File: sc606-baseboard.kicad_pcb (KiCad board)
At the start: 6 copper layers, 100 x 90 mm, 420 parts, among them IC1 TPS54561DPRT, IC2 TPS7A0518PDBVT, J1 PJ-202A, J10 WE_632723300011, J11 WE_632723300011, J12 U_FL-R-SMT-1_10_, J13 WE_632723300011, J14 CONMMCX002-SMD-T, J2 WE_68715014522, J3 F52R-1A7H1-11020, J4 46756-1001, J5 U_FL-R-SMT-1_10_, J6 U_FL-R-SMT-1_10_, J7 DM3AT-SF-PEJM5, J8 693022010811, J9 0473460001, M1 SC606T, Q1 BSS138APW, Q2 BSS138-7-F, Q3 BSS138APW, Q4 BSS138APW, Q5 BSS138APW, Q6 BSS138APW, Q7 BSS138-7-F, Q8 BSS138-7-F, SW1 1X03, U1 AP62301WU-7, U10 NCP163ASN330T1G, U11 EMIF06-MSD02N16, U12 FSUSB30MUX, U13 FT232RQ-REEL, U15 USB57442G, U2 AP62301WU-7, U3 AP62301WU-7, U4 74LVC1G123GN, U5 NTS0102GT, U6 PCA9547BS, U7 LT9611UXC, U8 NTS0102GT, U9 TPD13S523PWR, Y1 ABM8G-24.000MHZ-18-D2Y-T, Y2 ABM8G-25.000MHZ-B4Y-T

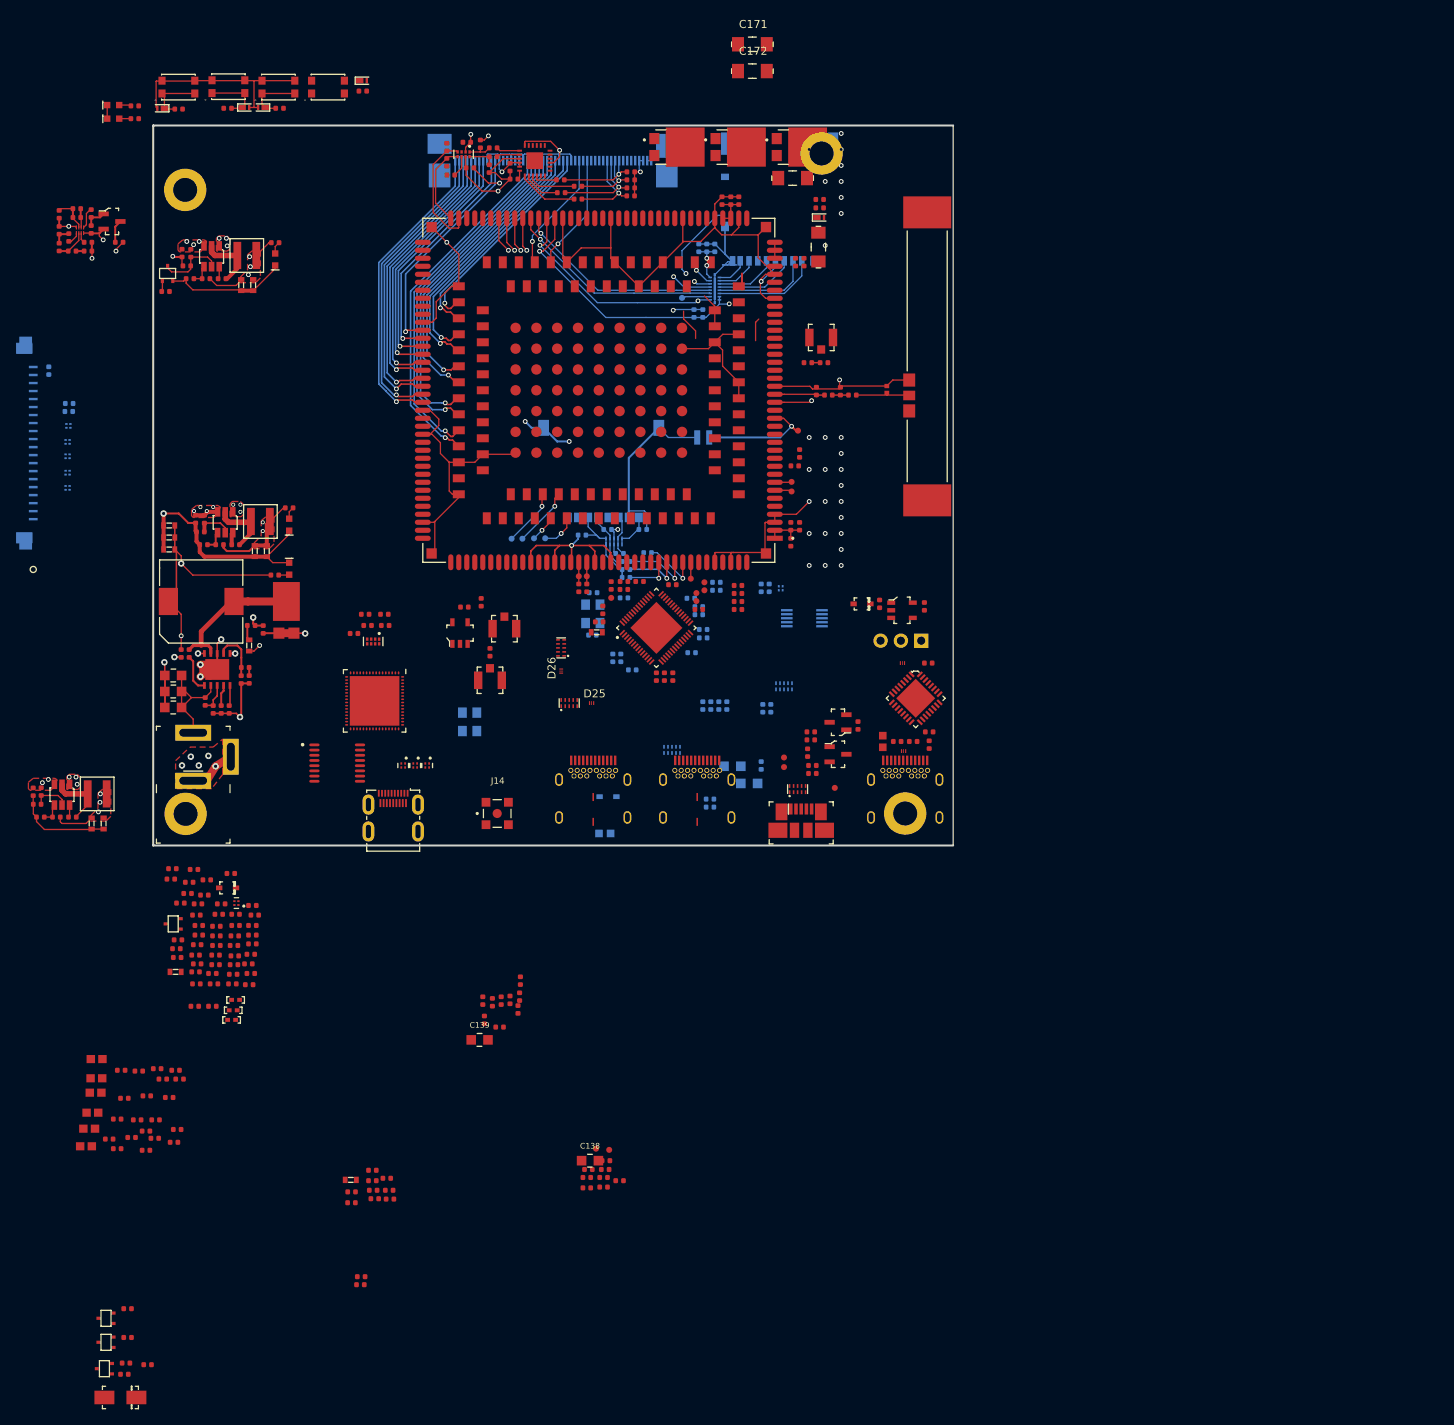
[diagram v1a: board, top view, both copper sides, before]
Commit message: All components placed on board
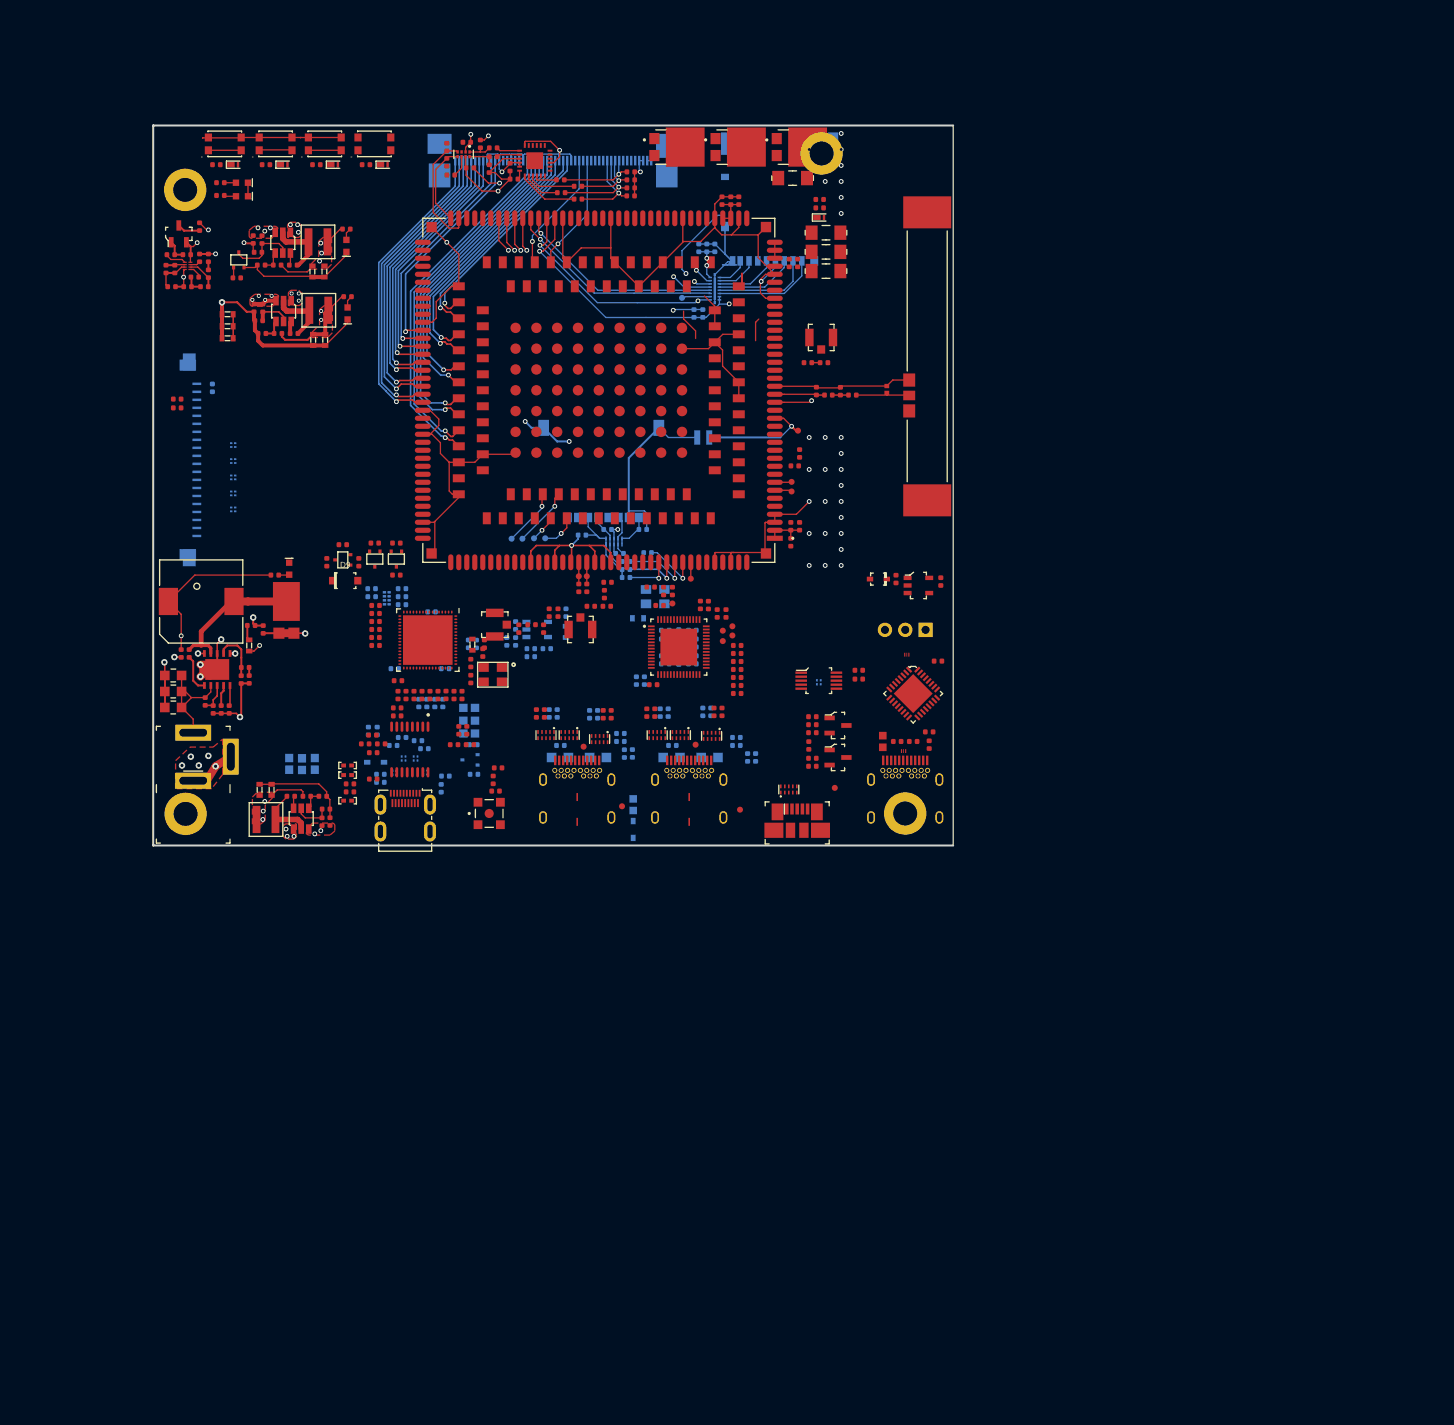
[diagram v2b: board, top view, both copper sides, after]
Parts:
- added C142: C_1u_0402, sc606-baseboard-footprints:0402-cap, F.Cu at (118.1, 120.3)
- added C143: C_1u_0402, sc606-baseboard-footprints:0402-cap, F.Cu at (117.8, 123.2)
- added R138: R_0R_0402, sc606-baseboard-footprints:0402-res, F.Cu at (124.5, 100.9)
- added R139: R_0R_0402, sc606-baseboard-footprints:0402-res, F.Cu at (125.6, 100.9)
- added R140: R_0R_0402, sc606-baseboard-footprints:0402-res, F.Cu at (117.5, 121.8)
- C102, C103, C120, C125, C131, C138, C139, C47, C48, C49, C50, C51, C52, C54, C55, C56, C59, C60, C61, C62, C63, C64, C65, C66, C67, C68, C70, C73, C74, C75, C76, C77, C78, C79, C80, C85, C86, C87, C88, C94, C95, C96, C99, D10, L13, L14, L15, L16, L17, L18, L19, L21, L5, L6, L7, Q3, R113, R122, R123, R124, R125, R131, R132, R134, R135, R71, R72, R73, R74, R81, R82, R84, R85, R89, R90, R92, R94, U10, U8: moved to B.Cu
- C108, C132, C133, C135, C148, C150, D31, D32, R107, R119, R55, R56, U12, Y1: moved to F.Cu
- D25, D26: value PESD5V0C2BDFZ -> PUSB3F96X_PASS; footprint sc606-baseboard-footprints:DFN0603-3 -> sc606-baseboard-footprints:PUSB3F96X
- D9: value S1G -> 1N4148W-7-F; footprint sc606-baseboard-footprints:DO-214AC -> antmicro-footprints:SOD-123
- moved D9 105.9 mm to (99.0, 96.9), turned to 0 degrees
- moved R80 105.8 mm to (98.7, 92.4)
- moved R79 105.6 mm to (100.7, 94.6), turned to 90 degrees
- moved Q4 105.4 mm to (98.7, 94.3)
- moved R78 104.8 mm to (105.4, 92.2)
- moved Q6 104.4 mm to (105.4, 94.2), turned to 270 degrees
- moved R83 102.8 mm to (96.7, 94.6), turned to 90 degrees
- moved Q5 100.7 mm to (102.7, 94.2), turned to 270 degrees
- moved R77 100.6 mm to (102.7, 92.2)
- moved C91 84.4 mm to (120.7, 102.9), turned to 270 degrees
- moved C89 84.1 mm to (123.8, 102.9), turned to 270 degrees
- moved R93 82.4 mm to (131.4, 98.6), turned to 270 degrees
- moved C93 81.8 mm to (131.8, 97.1)
- moved C98 78.6 mm to (131.7, 100.1)
- moved C101 76.8 mm to (129.7, 100.1)
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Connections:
- net /display module/SoMtoLT__SCL renamed /display module/SoMtoLT_SCL
- C103 pad 2: Net-(C103-Pad2) -> /USB_HUB_Connectors/5V0_USB
- C138 pad 2: Net-(C103-Pad2) -> /USB_HUB_Connectors/5V0_USB
- C139 pad 2: Net-(C103-Pad2) -> /USB_HUB_Connectors/5V0_USB
- C151 pad 2: Net-(C151-Pad2) -> /USB_HUB_Connectors/5V0_USB
- C169 pad 2: Net-(C151-Pad2) -> /USB_HUB_Connectors/5V0_USB
- C170 pad 2: Net-(C151-Pad2) -> /USB_HUB_Connectors/5V0_USB
- C171 pad 1: (no net) -> V_SOM
- C172 pad 1: (no net) -> V_SOM
- C89 pad 1: ANT-WIFI -> Net-(C89-Pad1)
- D25 pad 1: /USB_HUB_Connectors/USB_C1_D_P -> /USB_HUB_Connectors/USB_C1_D1_N
- D25 pad 2: /USB_HUB_Connectors/USB_C1_D_N -> /USB_HUB_Connectors/USB_C1_D1_P
- D26 pad 1: /USB_HUB_Connectors/USB_C2_D_P -> /USB_HUB_Connectors/USB_C2_SS_C_TX1_N
- D26 pad 2: /USB_HUB_Connectors/USB_C2_D_N -> /USB_HUB_Connectors/USB_C2_SS_C_TX1_P
- D27 pad 1: /USB_HUB_Connectors/USB_C1_SS_RX2_P -> /USB_HUB_Connectors/USB_C1_SS_C_TX2_N
- D27 pad 10: /USB_HUB_Connectors/USB_C1_SS_RX2_P -> /USB_HUB_Connectors/USB_C1_SS_C_TX2_N
- D27 pad 2: /USB_HUB_Connectors/USB_C1_SS_RX2_N -> /USB_HUB_Connectors/USB_C1_SS_C_TX2_P
- D27 pad 4: /USB_HUB_Connectors/USB_C1_SS_TX2_P -> /USB_HUB_Connectors/USB_C1_SS_C_RX2_P
- D27 pad 5: /USB_HUB_Connectors/USB_C1_SS_TX2_N -> /USB_HUB_Connectors/USB_C1_SS_C_RX2_N
- D27 pad 6: /USB_HUB_Connectors/USB_C1_SS_TX2_N -> /USB_HUB_Connectors/USB_C1_SS_C_RX2_N
- D27 pad 7: /USB_HUB_Connectors/USB_C1_SS_TX2_P -> /USB_HUB_Connectors/USB_C1_SS_C_RX2_P
- D27 pad 9: /USB_HUB_Connectors/USB_C1_SS_RX2_N -> /USB_HUB_Connectors/USB_C1_SS_C_TX2_P
- D28 pad 1: /USB_HUB_Connectors/USB_C1_SS_TX1_P -> /USB_HUB_Connectors/USB_C1_SS_C_TX1_N
- D28 pad 10: /USB_HUB_Connectors/USB_C1_SS_TX1_P -> /USB_HUB_Connectors/USB_C1_SS_C_TX1_N
- D28 pad 2: /USB_HUB_Connectors/USB_C1_SS_TX1_N -> /USB_HUB_Connectors/USB_C1_SS_C_TX1_P
- D28 pad 4: /USB_HUB_Connectors/USB_C1_SS_RX1_P -> /USB_HUB_Connectors/USB_C1_SS_C_RX1_N
- D28 pad 5: /USB_HUB_Connectors/USB_C1_SS_RX1_N -> /USB_HUB_Connectors/USB_C1_SS_C_RX1_P
- D28 pad 6: /USB_HUB_Connectors/USB_C1_SS_RX1_N -> /USB_HUB_Connectors/USB_C1_SS_C_RX1_P
- D28 pad 7: /USB_HUB_Connectors/USB_C1_SS_RX1_P -> /USB_HUB_Connectors/USB_C1_SS_C_RX1_N
- D28 pad 9: /USB_HUB_Connectors/USB_C1_SS_TX1_N -> /USB_HUB_Connectors/USB_C1_SS_C_TX1_P
- D31 pad 1: /USB_HUB_Connectors/USB_C2_SS_TX2_P -> /USB_HUB_Connectors/USB_C2_D1_N
- D31 pad 10: /USB_HUB_Connectors/USB_C2_SS_TX2_P -> /USB_HUB_Connectors/USB_C2_D1_N
- D31 pad 2: /USB_HUB_Connectors/USB_C2_SS_TX2_N -> /USB_HUB_Connectors/USB_C2_D1_P
- D31 pad 4: /USB_HUB_Connectors/USB_C2_SS_RX2_P -> /USB_HUB_Connectors/USB_C2_D2_N
- D31 pad 5: /USB_HUB_Connectors/USB_C2_SS_RX2_N -> /USB_HUB_Connectors/USB_C2_D2_P
- D31 pad 6: /USB_HUB_Connectors/USB_C2_SS_RX2_N -> /USB_HUB_Connectors/USB_C2_D2_P
- D31 pad 7: /USB_HUB_Connectors/USB_C2_SS_RX2_P -> /USB_HUB_Connectors/USB_C2_D2_N
- D31 pad 9: /USB_HUB_Connectors/USB_C2_SS_TX2_N -> /USB_HUB_Connectors/USB_C2_D1_P
- D32 pad 1: /USB_HUB_Connectors/USB_C2_SS_TX1_P -> /USB_HUB_Connectors/USB_C2_SS_C_TX2_N
- D32 pad 10: /USB_HUB_Connectors/USB_C2_SS_TX1_P -> /USB_HUB_Connectors/USB_C2_SS_C_TX2_N
- D32 pad 2: /USB_HUB_Connectors/USB_C2_SS_TX1_N -> /USB_HUB_Connectors/USB_C2_SS_C_TX2_P
- D32 pad 4: /USB_HUB_Connectors/USB_C2_SS_RX1_P -> /USB_HUB_Connectors/USB_C2_SS_C_RX2_P
- D32 pad 5: /USB_HUB_Connectors/USB_C2_SS_RX1_N -> /USB_HUB_Connectors/USB_C2_SS_C_RX2_N
- D32 pad 6: /USB_HUB_Connectors/USB_C2_SS_RX1_N -> /USB_HUB_Connectors/USB_C2_SS_C_RX2_N
- D32 pad 7: /USB_HUB_Connectors/USB_C2_SS_RX1_P -> /USB_HUB_Connectors/USB_C2_SS_C_RX2_P
- D32 pad 9: /USB_HUB_Connectors/USB_C2_SS_TX1_N -> /USB_HUB_Connectors/USB_C2_SS_C_TX2_P
- D8 pad 2: (no net) -> /display module/CEC_HDMI
- J11 pad A1: (no net) -> GND
- J11 pad A6: /USB_HUB_Connectors/USB_C1_D_P -> /USB_HUB_Connectors/USB_C1_D1_P
- J11 pad A7: /USB_HUB_Connectors/USB_C1_D_N -> /USB_HUB_Connectors/USB_C1_D1_N
- J11 pad B1: Net-(C103-Pad2) -> GND
- J11 pad B10: /USB_HUB_Connectors/USB_C1_SS_C_RX1_P -> /USB_HUB_Connectors/USB_C1_SS_C_RX1_N
- J11 pad B11: /USB_HUB_Connectors/USB_C1_SS_C_RX1_N -> /USB_HUB_Connectors/USB_C1_SS_C_RX1_P
- J11 pad B12: (no net) -> GND
- J11 pad B6: /USB_HUB_Connectors/USB_C1_D_P -> /USB_HUB_Connectors/USB_C1_D2_P
- J11 pad B7: /USB_HUB_Connectors/USB_C1_D_N -> /USB_HUB_Connectors/USB_C1_D2_N
- J13 pad A1: (no net) -> GND
- J13 pad A6: /USB_HUB_Connectors/USB_C2_D_P -> /USB_HUB_Connectors/USB_C2_D1_P
- J13 pad A7: /USB_HUB_Connectors/USB_C2_D_N -> /USB_HUB_Connectors/USB_C2_D1_N
- J13 pad B1: Net-(C151-Pad2) -> GND
- J13 pad B10: /USB_HUB_Connectors/USB_C2_SS_C_RX1_P -> /USB_HUB_Connectors/USB_C2_SS_C_RX1_N
- J13 pad B11: /USB_HUB_Connectors/USB_C2_SS_C_RX1_N -> /USB_HUB_Connectors/USB_C2_SS_C_RX1_P
- J13 pad B12: (no net) -> GND
- J13 pad B6: /USB_HUB_Connectors/USB_C2_D_P -> /USB_HUB_Connectors/USB_C2_D2_P
- J13 pad B7: /USB_HUB_Connectors/USB_C2_D_N -> /USB_HUB_Connectors/USB_C2_D2_N
- J14 pad 1: Net-(C91-Pad1) -> Net-(C143-Pad1)
- L16 pad 1: /display module/TX_D2_C_P -> /display module/TX_D2_C_N
- L16 pad 2: /display module/TX_D2_Ferr_P -> /display module/TX_D2_Ferr_N
- L16 pad 3: /display module/TX_D2_Ferr_N -> /display module/TX_D2_Ferr_P
- L16 pad 4: /display module/TX_D2_C_N -> /display module/TX_D2_C_P
- L17 pad 1: /display module/TX_D1_C_P -> /display module/TX_D1_C_N
- L17 pad 2: /display module/TX_D1_Ferr_P -> /display module/TX_D1_Ferr_N
- L17 pad 3: /display module/TX_D1_Ferr_N -> /display module/TX_D1_Ferr_P
- L17 pad 4: /display module/TX_D1_C_N -> /display module/TX_D1_C_P
- L18 pad 1: /display module/TX_D0_C_P -> /display module/TX_D0_C_N
- L18 pad 2: /display module/TX_D0_Ferr_P -> /display module/TX_D0_Ferr_N
- L18 pad 3: /display module/TX_D0_Ferr_N -> /display module/TX_D0_Ferr_P
- L18 pad 4: /display module/TX_D0_C_N -> /display module/TX_D0_C_P
- L19 pad 1: /display module/TX_CLK_C_P -> /display module/TX_CLK_C_N
- L19 pad 2: /display module/TX_CLK_Ferr_P -> /display module/TX_CLK_Ferr_N
- L19 pad 3: /display module/TX_CLK_Ferr_N -> /display module/TX_CLK_Ferr_P
- L19 pad 4: /display module/TX_CLK_C_N -> /display module/TX_CLK_C_P
- L22 pad 1: /USB_flash_debug/SoM_USB_Ferr_D_P -> /USB_flash_debug/SoM_USB_Ferr_D_N
- L22 pad 2: SoM_USB_D_P -> SoM_USB_D_N
- L22 pad 3: SoM_USB_D_N -> SoM_USB_D_P
- L22 pad 4: /USB_flash_debug/SoM_USB_Ferr_D_N -> /USB_flash_debug/SoM_USB_Ferr_D_P
- R126 pad 1: ANT-WIFI -> Net-(C89-Pad1)
- R130 pad 1: /USB_HUB_Connectors/USB_C1_SS_RX1_N -> /USB_HUB_Connectors/USB_C1_SS_RX1_P
- R130 pad 2: /USB_HUB_Connectors/USB_C1_SS_C_RX1_N -> /USB_HUB_Connectors/USB_C1_SS_C_RX1_P
- R133 pad 1: /USB_HUB_Connectors/USB_C1_SS_RX1_P -> /USB_HUB_Connectors/USB_C1_SS_RX1_N
- R133 pad 2: /USB_HUB_Connectors/USB_C1_SS_C_RX1_P -> /USB_HUB_Connectors/USB_C1_SS_C_RX1_N
- R136 pad 1: /USB_HUB_Connectors/USB_C2_SS_RX1_N -> /USB_HUB_Connectors/USB_C2_SS_RX1_P
- R136 pad 2: /USB_HUB_Connectors/USB_C2_SS_C_RX1_N -> /USB_HUB_Connectors/USB_C2_SS_C_RX1_P
- R137 pad 1: /USB_HUB_Connectors/USB_C2_SS_RX1_P -> /USB_HUB_Connectors/USB_C2_SS_RX1_N
- R137 pad 2: /USB_HUB_Connectors/USB_C2_SS_C_RX1_P -> /USB_HUB_Connectors/USB_C2_SS_C_RX1_N
- R50 pad 2: /display module/SoMtoLT__SDA -> /display module/SoMtoLT_SDA
- U15 pad 1: /USB_HUB_Connectors/USB_C1_D_P -> /USB_HUB_Connectors/USB_C1_D1_P
- U15 pad 17: /USB_HUB_Connectors/USB_C2_D_P -> /USB_HUB_Connectors/USB_C2_D1_P
- U15 pad 18: /USB_HUB_Connectors/USB_C2_D_N -> /USB_HUB_Connectors/USB_C2_D1_N
- U15 pad 2: /USB_HUB_Connectors/USB_C1_D_N -> /USB_HUB_Connectors/USB_C1_D1_N
- U15 pad 24: /USB_HUB_Connectors/USB_C2_D_P -> /USB_HUB_Connectors/USB_C2_D2_P
- U15 pad 25: /USB_HUB_Connectors/USB_C2_D_N -> /USB_HUB_Connectors/USB_C2_D2_N
- U15 pad 8: /USB_HUB_Connectors/USB_C1_D_P -> /USB_HUB_Connectors/USB_C1_D2_P
- U15 pad 9: /USB_HUB_Connectors/USB_C1_D_N -> /USB_HUB_Connectors/USB_C1_D2_N
- U7 pad 16: (no net) -> LT9611_VDD12
- U7 pad 19: /display module/SoMtoLT__SDA -> /display module/SoMtoLT_SDA
- U7 pad 31: (no net) -> LT9611_VDD12
- U7 pad 51: Net-(U7-Pad51) -> LT9611_VCC33_RX
- U7 pad 53: Net-(U7-Pad53) -> LT9611_VDD12
- U7 pad 54: Net-(U7-Pad53) -> LT9611_VDD12
- U7 pad 55: Net-(U7-Pad51) -> LT9611_VCC33_RX
- U8 pad 1: (no net) -> /display module/SoMtoLT_SDA
- U9 pad 11: /display module/TX_D2_Ferr_N -> /display module/TX_D0_Ferr_N
- U9 pad 12: /display module/TX_D2_Ferr_P -> /display module/TX_D0_Ferr_P
- U9 pad 15: /display module/TX_D0_Ferr_N -> /display module/TX_D2_Ferr_N
- U9 pad 16: /display module/TX_D0_Ferr_P -> /display module/TX_D2_Ferr_P
- U9 pad 9: (no net) -> /display module/TX_CLK_Ferr_N
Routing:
- net 5V0_SYS: track 63.9 -> 50.7 mm, vias 14 -> 13
- net GND: track 421.0 -> 409.1 mm, vias 62 -> 60
- net Net-(D11-PadK): track 7.41 -> 4.10 mm
- net Net-(D13-PadK): track 7.37 -> 4.10 mm
- net Net-(D12-PadK): track 7.42 -> 4.52 mm

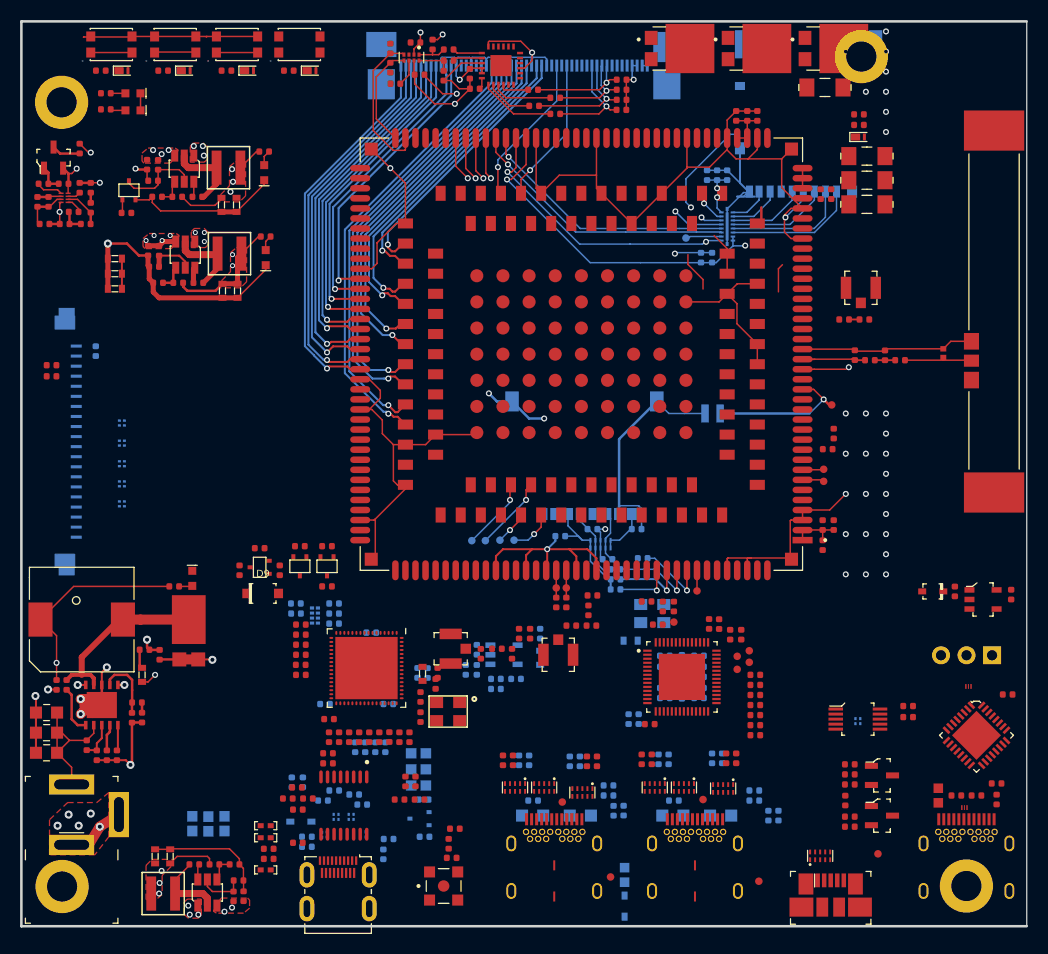
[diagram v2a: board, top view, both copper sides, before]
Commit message: Finished component placement
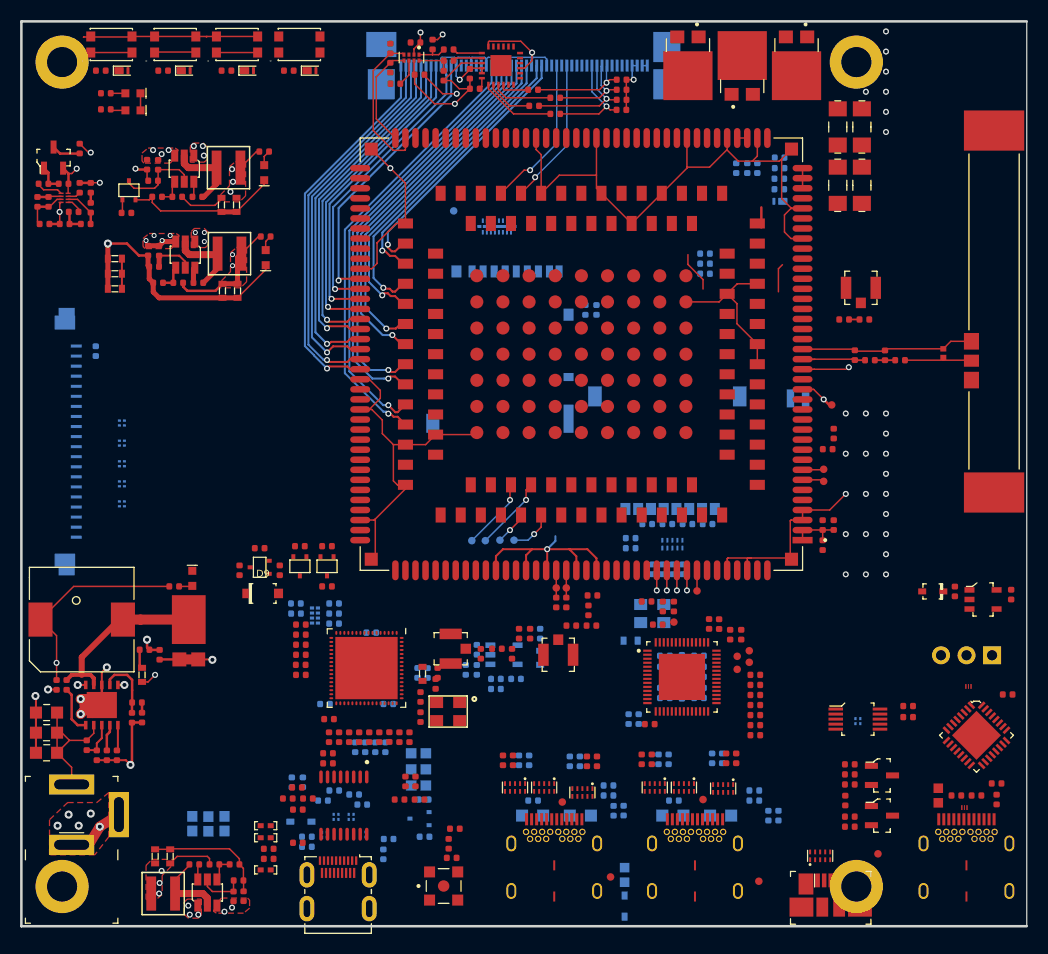
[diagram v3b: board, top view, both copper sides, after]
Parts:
- C10, C12, C3, C5, C7, C9, D1, R1, R55, R56: moved to B.Cu
- moved R55 60.1 mm to (135.6, 91.4)
- moved R56 60.1 mm to (135.6, 92.4)
- moved J7 38.6 mm to (122.6, 72.6), turned to 180 degrees
- moved TP11 23.3 mm to (118.0, 58.8)
- moved U11 22.9 mm to (122.3, 60.4), turned to 0 degrees
- moved C100 13.6 mm to (131.1, 68.7), turned to 270 degrees
- moved C97 11.6 mm to (132.2, 68.7), turned to 270 degrees
- moved MP3 11.0 mm to (158.0, 126.0)
- moved C5 10.2 mm to (150.4, 56.7), turned to 180 degrees
- moved C3 10.2 mm to (150.4, 55.6), turned to 180 degrees
- moved D1 10.1 mm to (150.4, 57.9), turned to 180 degrees
- moved C16 9.80 mm to (143.0, 65.1), turned to 180 degrees
- moved C14 8.88 mm to (143.0, 64.1), turned to 180 degrees
- moved C104 8.73 mm to (137.2, 90.0)
- moved C105 8.69 mm to (141.2, 90.0), turned to 0 degrees
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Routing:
- net GND: track 409.1 -> 350.0 mm, vias 60 -> 56
- net SD_DATA_6: track 42.5 -> 4.05 mm, vias 3 -> 0
- net SD_LDO11: track 40.1 -> 2.87 mm, vias 3 -> 0
- net SD_DATA_4: track 31.7 -> 0.00 mm, vias 2 -> 0
- net SD_DATA_5: track 30.8 -> 0.00 mm, vias 2 -> 0
- net SD_DATA_0: track 29.6 -> 0.00 mm, vias 2 -> 0
- net SD_DATA_1: track 29.2 -> 0.00 mm, vias 2 -> 0
- net SD_DATA_2: track 27.1 -> 0.00 mm, vias 1 -> 0
- net SD_DATA_3: track 26.1 -> 0.00 mm, vias 1 -> 0
- net Net-(J7-Pad1): track 13.0 -> 0.00 mm
- net Net-(J7-Pad2): track 12.1 -> 0.00 mm
- net Net-(C104-Pad1): track 12.1 -> 0.00 mm
- net RTC_BAT: track 14.4 -> 3.54 mm
- net Net-(J7-Pad3): track 9.85 -> 0.00 mm
- net USIM1_VDD: track 10.2 -> 2.14 mm
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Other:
- net class CSI_DSI_Inner: clearance 0.508 -> 0.15
- net class CSI_DSI_Outer: clearance 0.508 -> 0.15
